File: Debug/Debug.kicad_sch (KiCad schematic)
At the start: 54 parts

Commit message: Updated debug card...
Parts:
- D1: value (none) -> RDY; footprint (none) -> LED_THT:LED_D5.0mm
- D10: renamed from D?; value (none) -> Sync; footprint (none) -> LED_THT:LED_D5.0mm
- D11: renamed from D?; value (none) -> RW; footprint (none) -> LED_THT:LED_D5.0mm
- D12: renamed from D?; value (none) -> Reset; footprint (none) -> LED_THT:LED_D5.0mm
- D13: renamed from D?; value (none) -> IRQ; footprint (none) -> LED_THT:LED_D5.0mm
- D14: renamed from D?; value (none) -> NMI; footprint (none) -> LED_THT:LED_D5.0mm
- D15: renamed from D?; value (none) -> PHI1; footprint (none) -> LED_THT:LED_D5.0mm
- D16: renamed from D?; value (none) -> PHI2; footprint (none) -> LED_THT:LED_D5.0mm
- D2: value (none) -> Sync; footprint (none) -> LED_THT:LED_D5.0mm
- D3: value (none) -> RW; footprint (none) -> LED_THT:LED_D5.0mm
- D4: value (none) -> Reset; footprint (none) -> LED_THT:LED_D5.0mm
- D5: value (none) -> IRQ; footprint (none) -> LED_THT:LED_D5.0mm
- D6: value (none) -> NMI; footprint (none) -> LED_THT:LED_D5.0mm
- D7: value (none) -> PHI1; footprint (none) -> LED_THT:LED_D5.0mm
- D8: value (none) -> PHI2; footprint (none) -> LED_THT:LED_D5.0mm
- D9: renamed from D?; value (none) -> RDY; footprint (none) -> LED_THT:LED_D5.0mm
- R1: value (none) -> 270; footprint (none) -> Resistor_THT:R_Axial_DIN0207_L6.3mm_D2.5mm_P7.62mm_Horizontal
- R10, R11, R12, R13, R14, R15, R16, R17: renamed from R?; value (none) -> 220; footprint (none) -> Resistor_THT:R_Axial_DIN0207_L6.3mm_D2.5mm_P7.62mm_Horizontal
- R2, R3, R4, R5, R6, R7, R8, R9: value (none) -> 220; footprint (none) -> Resistor_THT:R_Axial_DIN0207_L6.3mm_D2.5mm_P7.62mm_Horizontal
- SW1: value (none) -> Step; footprint (none) -> Button_Switch_THT:SW_Push_2P1T_Toggle_CK_PVA1xxH1xxxxxxV2
- SW2: value (none) -> PHI1/Step; footprint (none) -> Button_Switch_THT:SW_Slide_1P2T_CK_OS102011MS2Q
- SW3: value (none) -> Run; footprint (none) -> Button_Switch_THT:SW_DIP_SPSTx01_Slide_9.78x4.72mm_W7.62mm_P2.54mm
- SW4: value (none) -> SI/SC; footprint (none) -> Button_Switch_THT:SW_Slide_1P2T_CK_OS102011MS2Q
- U1: value (none) -> 74LS04; footprint (none) -> Package_DIP:DIP-14_W7.62mm_Socket_LongPads
- U10, U12, U14, U3, U6, U8: value (none) -> MC14495P1; footprint (none) -> Package_DIP:DIP-16_W7.62mm_Socket_LongPads
- U11, U13, U15, U4, U7, U9: value (none) -> HDSP-7803; footprint (none) -> Display_7Segment:HDSP-7801
- U16: renamed from U?; value (none) -> 74LS374; footprint (none) -> Package_DIP:DIP-20_W7.62mm_Socket_LongPads
- U2: value (none) -> 74LS74; footprint (none) -> Package_DIP:DIP-14_W7.62mm_Socket_LongPads
- U5: value (none) -> 74LS374; footprint (none) -> Package_DIP:DIP-20_W7.62mm_Socket_LongPads
- gave numbers to parts that had none: 1
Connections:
- net Reset renamed RESET
- net Sync renamed SYNC
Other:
- company: WolfNet -> WolfNet Computing

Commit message: Debug card layout completed...
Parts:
- removed D10: Sync, LED_THT:LED_D5.0mm, symbol Debug-rescue:LED-Generic_Device
- removed D11: RW, LED_THT:LED_D5.0mm, symbol Debug-rescue:LED-Generic_Device
- removed D12: Reset, LED_THT:LED_D5.0mm, symbol Debug-rescue:LED-Generic_Device
- removed D13: IRQ, LED_THT:LED_D5.0mm, symbol Debug-rescue:LED-Generic_Device
- removed D14: NMI, LED_THT:LED_D5.0mm, symbol Debug-rescue:LED-Generic_Device
- removed D15: PHI1, LED_THT:LED_D5.0mm, symbol Debug-rescue:LED-Generic_Device
- removed D16: PHI2, LED_THT:LED_D5.0mm, symbol Debug-rescue:LED-Generic_Device
- removed D9: RDY, LED_THT:LED_D5.0mm, symbol Debug-rescue:LED-Generic_Device
- removed R10, R11, R12, R13, R14, R15, R16, R17: 220, Resistor_THT:R_Axial_DIN0207_L6.3mm_D2.5mm_P7.62mm_Horizontal, symbol Debug-rescue:R-Generic_Device
- removed U16: 74LS374, Package_DIP:DIP-20_W7.62mm_Socket_LongPads, symbol 74xx:74LS374
- J1: footprint (none) -> Connector_PinHeader_2.54mm:PinHeader_2x19_P2.54mm_Horizontal
- U1: value 74LS04 -> 74HCT04
- U2: value 74LS74 -> 74HCT74
- U5: value 74LS374 -> 74HCT374
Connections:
- net NMI is gone; now on net ~{IRQ}: U5.13 (D4)
- net PHI0 is gone; now on net CLK: U5.14 (D5)
- net RESET is gone; now on net ~{RESET}: U5.8 (D3)
- net A0: now also J1.5 (Pin_5)
- net A1: now also J1.7 (Pin_7)
- net A10: now also J1.25 (Pin_25)
- net A11: now also J1.27 (Pin_27)
- net A12: now also J1.29 (Pin_29)
- net A13: now also J1.31 (Pin_31)
- net A14: now also J1.33 (Pin_33)
- net A15: now also J1.35 (Pin_35)
- net A2: now also J1.9 (Pin_9)
- net A3: now also J1.11 (Pin_11)
- net A4: now also J1.13 (Pin_13)
- net A5: now also J1.15 (Pin_15)
- net A6: now also J1.17 (Pin_17)
- net A7: now also J1.19 (Pin_19)
- net A8: now also J1.21 (Pin_21)
- net A9: now also J1.23 (Pin_23)
- net D0: now also J1.2 (Pin_2)
- net D1: now also J1.4 (Pin_4)
- net D2: now also J1.6 (Pin_6)
- net D3: now also J1.8 (Pin_8)
- net D4: now also J1.10 (Pin_10)
- net D5: now also J1.12 (Pin_12)
- net D6: now also J1.14 (Pin_14)
- net D7: now also J1.16 (Pin_16)
- net GND: now also J1.3 (Pin_3)
- net PHI1: now also J1.22 (Pin_22)
- net PHI2: now also J1.24 (Pin_24)
- net RDY: now also J1.30 (Pin_30)
- net SYNC: now also J1.32 (Pin_32)
- net VCC: now reaches J1.1
- net ~{RESET}: now reaches J1.18 (Pin_18)
- net CLK: now reaches J1.20 (Pin_20)
- net 8MHz: now reaches J1.26 (Pin_26)
- net ~{IRQ}: now reaches J1.34 (Pin_34)
- net +12v: now reaches J1.36 (Pin_36)
- net R\~{W}: now reaches J1.37 (Pin_37)
- net -12v: now reaches J1.38 (Pin_38)
- net R~{W} renamed R/~{W}
- no-connect marks 24 -> 25
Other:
- moved on the sheet: U14

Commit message: 98 unrouted traces...
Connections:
- net VCC is gone; now on net +5V: J1.1
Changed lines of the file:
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@@
+    (stroke (width 0) (type default) (color 0 0 0 0))
+  )
+  (wire (pts (xy 149.86 128.27) (xy 156.21 128.27))
     (stroke (width 0) (type default) (color 0 0 0 0))
   )
@@
   )
   (wire (pts (xy 212.09 34.29) (xy 212.09 48.26))
+    (stroke (width 0) (type default) (color 0 0 0 0))
+  )
+  (wire (pts (xy 149.86 125.73) (xy 156.21 125.73))
     (stroke (width 0) (type default) (color 0 0 0 0))
   )
@@
     )
   )
-  (global_label "VCC" (shape output) (at 156.21 125.73 180) (fields_autoplaced)
-    (effects (font (size 1.27 1.27)) (justify right))
-    (property "Intersheet References" "${INTERSHEET_REFS}" (id 0) (at 150.2572 125.6506 0)
-      (effects (font (size 1.27 1.27)) (justify right) hide)
-    )
-  )
   (global_label "A14" (shape input) (at 156.21 166.37 180) (fields_autoplaced)
     (effects (font (size 1.27 1.27)) (justify right))
@@
     (property "Intersheet References" "${INTERSHEET_REFS}" (id 0) (at 0 -1.27 0)
       (effects (font (size 1.27 1.27)) hide)
-    )
-  )
-  (global_label "GND" (shape input) (at 156.21 128.27 180) (fields_autoplaced)
-    (effects (font (size 1.27 1.27)) (justify right))
-    (property "Intersheet References" "${INTERSHEET_REFS}" (id 0) (at 150.0153 128.1906 0)
-      (effects (font (size 1.27 1.27)) (justify right) hide)
     )
   )
@@
     (pin "9")
   )
+  (symbol (lib_id "power:GND") (at 149.86 128.27 0) (unit 1)
+    (in_bom yes) (on_board yes)
+    (property "Reference" "#PWR?" (id 0) (at 149.86 134.62 0)
+      (effects (font (size 1.27 1.27)) hide)
+    )
+    (property "Value" "GND" (id 1) (at 149.987 132.6642 0))
+    (property "Footprint" "" (id 2) (at 149.86 128.27 0)
+      (effects (font (size 1.27 1.27)) hide)
+    )
+    (property "Datasheet" "" (id 3) (at 149.86 128.27 0)
+      (effects (font (size 1.27 1.27)) hide)
+    )
+    (pin "1")
+  )
+  (symbol (lib_id "power:+5V") (at 149.86 125.73 0) (unit 1)
+    (in_bom yes) (on_board yes)
+    (property "Reference" "#PWR?" (id 0) (at 149.86 129.54 0)
+      (effects (font (size 1.27 1.27)) hide)
+    )
+    (property "Value" "+5V" (id 1) (at 149.86 121.92 0))
+    (property "Footprint" "" (id 2) (at 149.86 125.73 0)
+      (effects (font (size 1.27 1.27)) hide)
+    )
+    (property "Datasheet" "" (id 3) (at 149.86 125.73 0)
+      (effects (font (size 1.27 1.27)) hide)
+    )
+    (pin "1")
+  )
   (sheet_instances
     (path "/" (page "1"))
@@
       (reference "#PWR0135") (unit 1) (value "+5V") (footprint "")
     )
+    (path "/1dc9ba2a-69c0-42e3-a4c2-6901de1d5d49"
+      (reference "#PWR?") (unit 1) (value "GND") (footprint "")
+    )
+    (path "/b118dd9e-05e2-402c-8b56-7c9265857475"
+      (reference "#PWR?") (unit 1) (value "+5V") (footprint "")
+    )
     (path "/00000000-0000-0000-0000-00006102ae1c"

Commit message: 90 unrouted traces...
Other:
- title: Debug Card -> WolfNet 6502 WBC - Debug Card
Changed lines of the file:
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@@
   (paper "A3")
   (title_block
-    (title "Debug Card")
+    (title "WolfNet 6502 WBC - Debug Card")
     (date "2022-05-17")
     (rev "1.0")

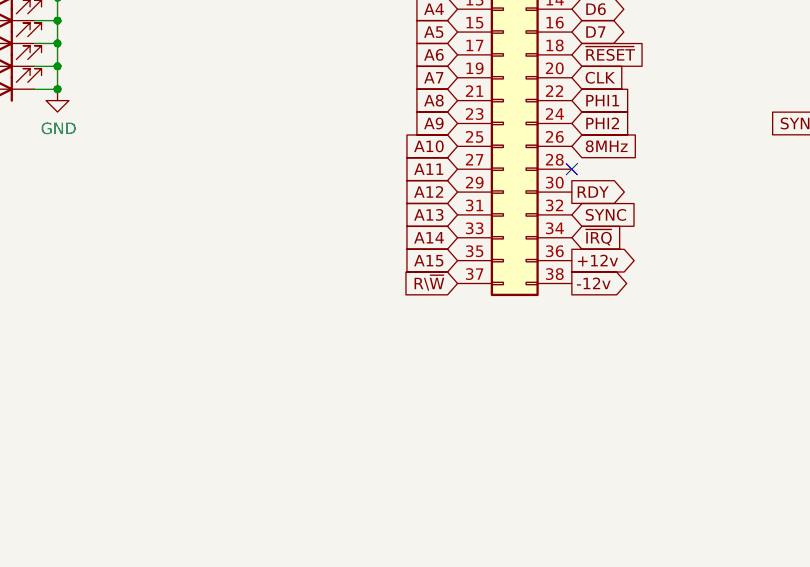
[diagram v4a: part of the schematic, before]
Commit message: 64 unrouted traces...
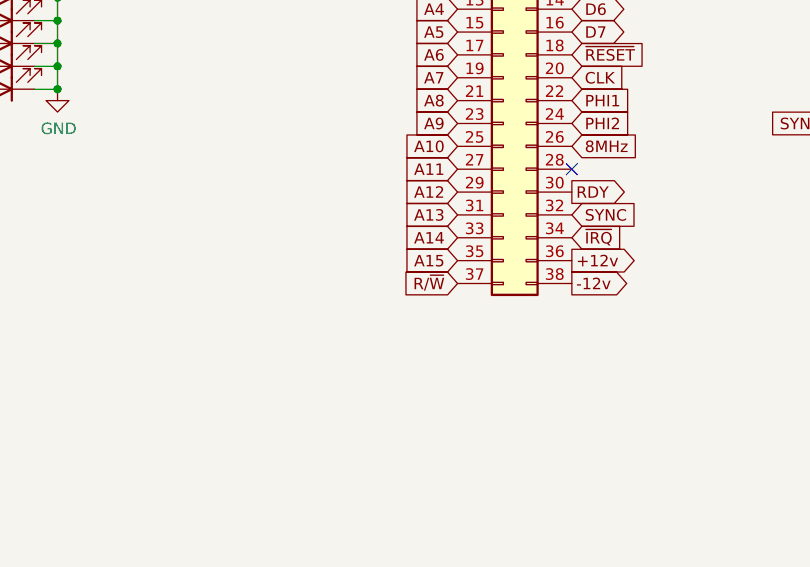
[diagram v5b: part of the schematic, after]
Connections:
- net R\~{W} is gone; now on net R/~{W}: J1.37 (Pin_37)
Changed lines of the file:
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@@
     )
   )
-  (global_label "R\\~{W}" (shape input) (at 156.21 171.45 180) (fields_autoplaced)
+  (global_label "R{slash}~{W}" (shape input) (at 156.21 171.45 180) (fields_autoplaced)
     (effects (font (size 1.27 1.27)) (justify right))
-    (property "Intersheet References" "${INTERSHEET_REFS}" (id 0) (at -438.15 -161.29 0)
-      (effects (font (size 1.27 1.27)) hide)
+    (property "Intersheet References" "${INTERSHEET_REFS}" (id 0) (at 149.8339 171.3706 0)
+      (effects (font (size 1.27 1.27)) (justify right) hide)
     )
   )
@@
   (symbol (lib_id "power:GND") (at 149.86 128.27 0) (unit 1)
     (in_bom yes) (on_board yes)
-    (property "Reference" "#PWR?" (id 0) (at 149.86 134.62 0)
+    (property "Reference" "#PWR0101" (id 0) (at 149.86 134.62 0)
       (effects (font (size 1.27 1.27)) hide)
     )
@@
   (symbol (lib_id "power:+5V") (at 149.86 125.73 0) (unit 1)
     (in_bom yes) (on_board yes)
-    (property "Reference" "#PWR?" (id 0) (at 149.86 129.54 0)
+    (property "Reference" "#PWR0102" (id 0) (at 149.86 129.54 0)
       (effects (font (size 1.27 1.27)) hide)
     )
@@
   )
   (symbol_instances
+    (path "/1dc9ba2a-69c0-42e3-a4c2-6901de1d5d49"
+      (reference "#PWR0101") (unit 1) (value "GND") (footprint "")
+    )
+    (path "/b118dd9e-05e2-402c-8b56-7c9265857475"
+      (reference "#PWR0102") (unit 1) (value "+5V") (footprint "")
+    )
     (path "/00000000-0000-0000-0000-000060f72f97"
       (reference "#PWR0103") (unit 1) (value "GND") (footprint "")
@@
       (reference "#PWR0135") (unit 1) (value "+5V") (footprint "")
     )
-    (path "/1dc9ba2a-69c0-42e3-a4c2-6901de1d5d49"
-      (reference "#PWR?") (unit 1) (value "GND") (footprint "")
-    )
-    (path "/b118dd9e-05e2-402c-8b56-7c9265857475"
-      (reference "#PWR?") (unit 1) (value "+5V") (footprint "")
-    )
     (path "/00000000-0000-0000-0000-00006102ae1c"

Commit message: Update Debug.kicad_sch
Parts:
- removed SW3: Run, Button_Switch_THT:SW_DIP_SPSTx01_Slide_9.78x4.72mm_W7.62mm_P2.54mm, symbol Switch:SW_SPST
- added SW?: Run, Button_Switch_THT:SW_Slide_1P2T_CK_OS102011MS2Q, symbol Switch:SW_SPDT
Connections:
- net GND: now also SW?.3 (C)
- net at U2.10 (~{S}): now also SW?.2 (B)
- no-connect marks 25 -> 26
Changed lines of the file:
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@@
   (no_connect (at 346.71 48.26))
   (no_connect (at 140.97 208.28))
+  (no_connect (at 274.32 143.51))
   (no_connect (at 233.68 46.99))
   (no_connect (at 224.79 48.26))
@@
     (pin "7")
   )
-  (symbol (lib_id "Switch:SW_SPST") (at 269.24 146.05 0) (unit 1)
-    (in_bom yes) (on_board yes)
-    (property "Reference" "SW3" (id 0) (at 269.24 140.081 0))
-    (property "Value" "Run" (id 1) (at 269.24 142.3924 0))
-    (property "Footprint" "Button_Switch_THT:SW_DIP_SPSTx01_Slide_9.78x4.72mm_W7.62mm_P2.54mm" (id 2) (at 269.24 146.05 0)
-      (effects (font (size 1.27 1.27)) hide)
-    )
-    (property "Datasheet" "~" (id 3) (at 269.24 146.05 0)
-      (effects (font (size 1.27 1.27)) hide)
-    )
-    (pin "1")
-    (pin "2")
-  )
-  (symbol (lib_id "power:GND") (at 274.32 146.05 0) (unit 1)
-    (in_bom yes) (on_board yes)
-    (property "Reference" "#PWR0104" (id 0) (at 274.32 152.4 0)
-      (effects (font (size 1.27 1.27)) hide)
-    )
-    (property "Value" "GND" (id 1) (at 274.447 150.4442 0))
-    (property "Footprint" "" (id 2) (at 274.32 146.05 0)
-      (effects (font (size 1.27 1.27)) hide)
-    )
-    (property "Datasheet" "" (id 3) (at 274.32 146.05 0)
+  (symbol (lib_id "power:GND") (at 274.32 148.59 0) (unit 1)
+    (in_bom yes) (on_board yes)
+    (property "Reference" "#PWR0104" (id 0) (at 274.32 154.94 0)
+      (effects (font (size 1.27 1.27)) hide)
+    )
+    (property "Value" "GND" (id 1) (at 274.447 152.9842 0))
+    (property "Footprint" "" (id 2) (at 274.32 148.59 0)
+      (effects (font (size 1.27 1.27)) hide)
+    )
+    (property "Datasheet" "" (id 3) (at 274.32 148.59 0)
       (effects (font (size 1.27 1.27)) hide)
     )
@@
     (pin "9")
   )
+  (symbol (lib_id "Switch:SW_SPDT") (at 269.24 146.05 0) (unit 1)
+    (in_bom yes) (on_board yes)
+    (property "Reference" "SW?" (id 0) (at 269.24 138.811 0))
+    (property "Value" "Run" (id 1) (at 269.24 141.1224 0))
+    (property "Footprint" "Button_Switch_THT:SW_Slide_1P2T_CK_OS102011MS2Q" (id 2) (at 269.24 146.05 0)
+      (effects (font (size 1.27 1.27)) hide)
+    )
+    (property "Datasheet" "~" (id 3) (at 269.24 146.05 0)
+      (effects (font (size 1.27 1.27)) hide)
+    )
+    (pin "1")
+    (pin "2")
+    (pin "3")
+  )
   (symbol (lib_id "power:GND") (at 149.86 128.27 0) (unit 1)
     (in_bom yes) (on_board yes)
@@
       (reference "SW2") (unit 1) (value "PHI1/Step") (footprint "Button_Switch_THT:SW_Slide_1P2T_CK_OS102011MS2Q")
     )
-    (path "/00000000-0000-0000-0000-000060f7634b"
-      (reference "SW3") (unit 1) (value "Run") (footprint "Button_Switch_THT:SW_DIP_SPSTx01_Slide_9.78x4.72mm_W7.62mm_P2.54mm")
-    )
     (path "/00000000-0000-0000-0000-000060f71734"
       (reference "SW4") (unit 1) (value "SI/SC") (footprint "Button_Switch_THT:SW_Slide_1P2T_CK_OS102011MS2Q")
     )
+    (path "/0aef16fa-9555-438d-87b3-458412edf5a2"
+      (reference "SW?") (unit 1) (value "Run") (footprint "Button_Switch_THT:SW_Slide_1P2T_CK_OS102011MS2Q")
+    )
     (path "/00000000-0000-0000-0000-000060f67b64"
